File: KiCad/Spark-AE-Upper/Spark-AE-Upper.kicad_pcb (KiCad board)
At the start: 2 copper layers, 0 parts

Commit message: bumping copyright year
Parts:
- added RP1: RK09K1130D62, easyeda2kicad:RES-TH_RK09K1130AAU, F.Cu at (125.5, 77.5)
- added RP2: RK09K1130D62, easyeda2kicad:RES-TH_RK09K1130AAU, F.Cu at (139.5, 77.5)

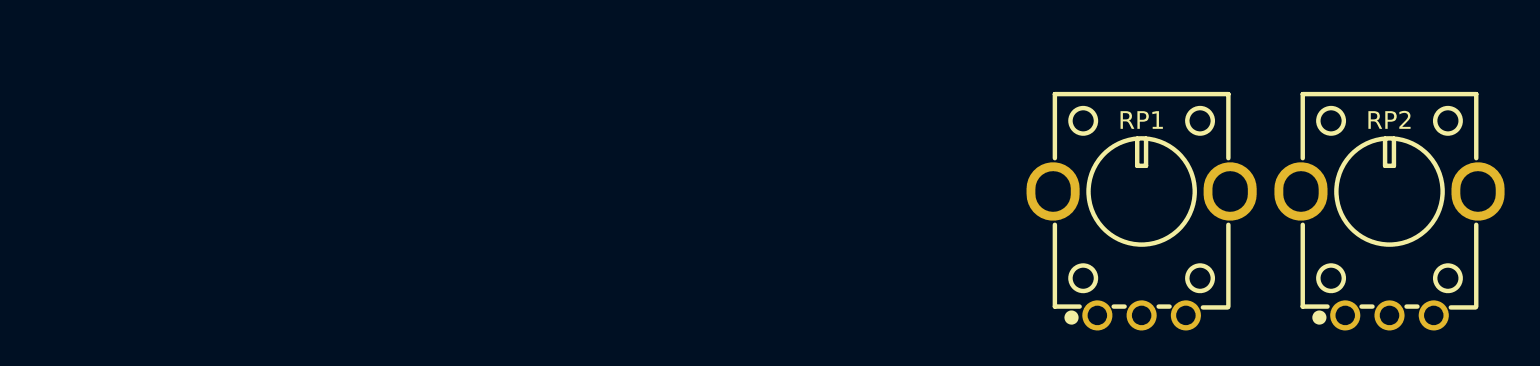
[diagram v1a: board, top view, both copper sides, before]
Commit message: updated to use components from clectric-diy's library
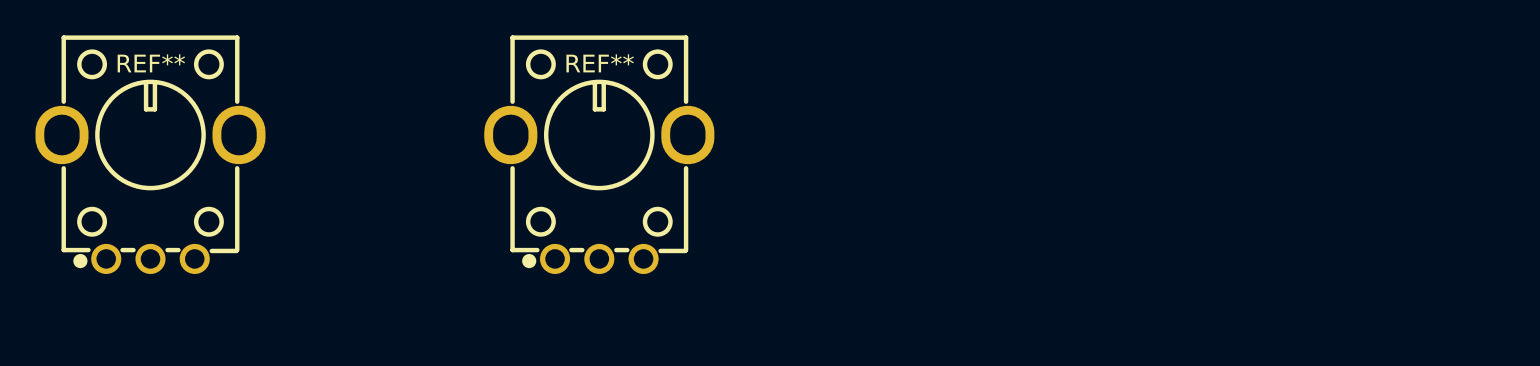
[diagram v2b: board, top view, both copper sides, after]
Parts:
- removed RP1, RP2: RK09K1130D62, easyeda2kicad:RES-TH_RK09K1130AAU
- added REF**: RES-TH_RK09K1130AAU, clectric-diy:RES-TH_RK09K1130AAU, F.Cu at (94.9, 74.3)
- added REF**: RES-TH_RK09K1130AAU, clectric-diy:RES-TH_RK09K1130AAU, F.Cu at (69.5, 74.3)
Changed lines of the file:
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@@
 	)
 	(net 0 "")
-	(net 1 "unconnected-(RP1-Pad2)")
-	(net 2 "unconnected-(RP1-Pad5)")
-	(net 3 "unconnected-(RP1-Pad1)")
-	(net 4 "unconnected-(RP1-Pad4)")
-	(net 5 "unconnected-(RP1-Pad3)")
-	(net 6 "unconnected-(RP2-Pad4)")
-	(net 7 "unconnected-(RP2-Pad1)")
-	(net 8 "unconnected-(RP2-Pad5)")
-	(net 9 "unconnected-(RP2-Pad3)")
-	(net 10 "unconnected-(RP2-Pad2)")
-	(footprint "easyeda2kicad:RES-TH_RK09K1130AAU"
+	(footprint "clectric-diy:RES-TH_RK09K1130AAU"
 		(layer "F.Cu")
-		(at 125.5 77.5)
-		(property "Reference" "RP1"
+		(at 94.87 74.31)
+		(property "Reference" "REF**"
 			(at 0 -7.5 0)
 			(layer "F.SilkS")
@@
 			)
 		)
-		(property "Value" "RK09K1130D62"
+		(property "Value" "RES-TH_RK09K1130AAU"
 			(at 0 7.5 0)
 			(layer "F.Fab")
@@
 			)
 		)
-		(property "LCSC Part" "C470399"
-			(at 0 0 0)
-			(unlocked yes)
-			(layer "F.Fab")
-			(hide yes)
-			(effects
-				(font
-					(size 1 1)
-					(thickness 0.15)
-				)
-			)
-		)
-		(sheetname "/")
-		(sheetfile "Spark-AE-Upper.kicad_sch")
 		(attr through_hole)
 		(fp_line
@@
 			(layers "*.Cu" "*.Mask")
 			(remove_unused_layers no)
-			(net 3 "unconnected-(RP1-Pad1)")
-			(pinfunction "1")
-			(pintype "unspecified")
 		)
 		(pad "2" thru_hole circle
@@
 			(layers "*.Cu" "*.Mask")
 			(remove_unused_layers no)
-			(net 1 "unconnected-(RP1-Pad2)")
-			(pinfunction "2")
-			(pintype "unspecified")
 		)
 		(pad "3" thru_hole circle
@@
 			(layers "*.Cu" "*.Mask")
 			(remove_unused_layers no)
-			(net 5 "unconnected-(RP1-Pad3)")
-			(pinfunction "3")
-			(pintype "unspecified")
 		)
 		(pad "4" thru_hole oval
@@
 			(layers "*.Cu" "*.Mask")
 			(remove_unused_layers no)
-			(net 4 "unconnected-(RP1-Pad4)")
-			(pinfunction "4")
-			(pintype "unspecified")
 		)
 		(pad "5" thru_hole oval
@@
 			(layers "*.Cu" "*.Mask")
 			(remove_unused_layers no)
-			(net 2 "unconnected-(RP1-Pad5)")
-			(pinfunction "5")
-			(pintype "unspecified")
 		)
 		(embedded_fonts no)
@@
 		)
 	)
-	(footprint "easyeda2kicad:RES-TH_RK09K1130AAU"
+	(footprint "clectric-diy:RES-TH_RK09K1130AAU"
 		(layer "F.Cu")
-		(at 139.5 77.5)
-		(property "Reference" "RP2"
+		(at 69.52 74.31)
+		(property "Reference" "REF**"
 			(at 0 -7.5 0)
 			(layer "F.SilkS")
@@
 			)
 		)
-		(property "Value" "RK09K1130D62"
+		(property "Value" "RES-TH_RK09K1130AAU"
 			(at 0 7.5 0)
 			(layer "F.Fab")
@@
 			)
 		)
-		(property "LCSC Part" "C470399"
-			(at 0 0 0)
-			(unlocked yes)
-			(layer "F.Fab")
-			(hide yes)
-			(effects
-				(font
-					(size 1 1)
-					(thickness 0.15)
-				)
-			)
-		)
-		(sheetname "/")
-		(sheetfile "Spark-AE-Upper.kicad_sch")
 		(attr through_hole)
 		(fp_line
@@
 			(layers "*.Cu" "*.Mask")
 			(remove_unused_layers no)
-			(net 7 "unconnected-(RP2-Pad1)")
-			(pinfunction "1")
-			(pintype "unspecified")
 		)
 		(pad "2" thru_hole circle
@@
 			(layers "*.Cu" "*.Mask")
 			(remove_unused_layers no)
-			(net 10 "unconnected-(RP2-Pad2)")
-			(pinfunction "2")
-			(pintype "unspecified")
 		)
 		(pad "3" thru_hole circle
@@
 			(layers "*.Cu" "*.Mask")
 			(remove_unused_layers no)
-			(net 9 "unconnected-(RP2-Pad3)")
-			(pinfunction "3")
-			(pintype "unspecified")
 		)
 		(pad "4" thru_hole oval
@@
 			(layers "*.Cu" "*.Mask")
 			(remove_unused_layers no)
-			(net 6 "unconnected-(RP2-Pad4)")
-			(pinfunction "4")
-			(pintype "unspecified")
 		)
 		(pad "5" thru_hole oval
@@
 			(layers "*.Cu" "*.Mask")
 			(remove_unused_layers no)
-			(net 8 "unconnected-(RP2-Pad5)")
-			(pinfunction "5")
-			(pintype "unspecified")
 		)
 		(embedded_fonts no)

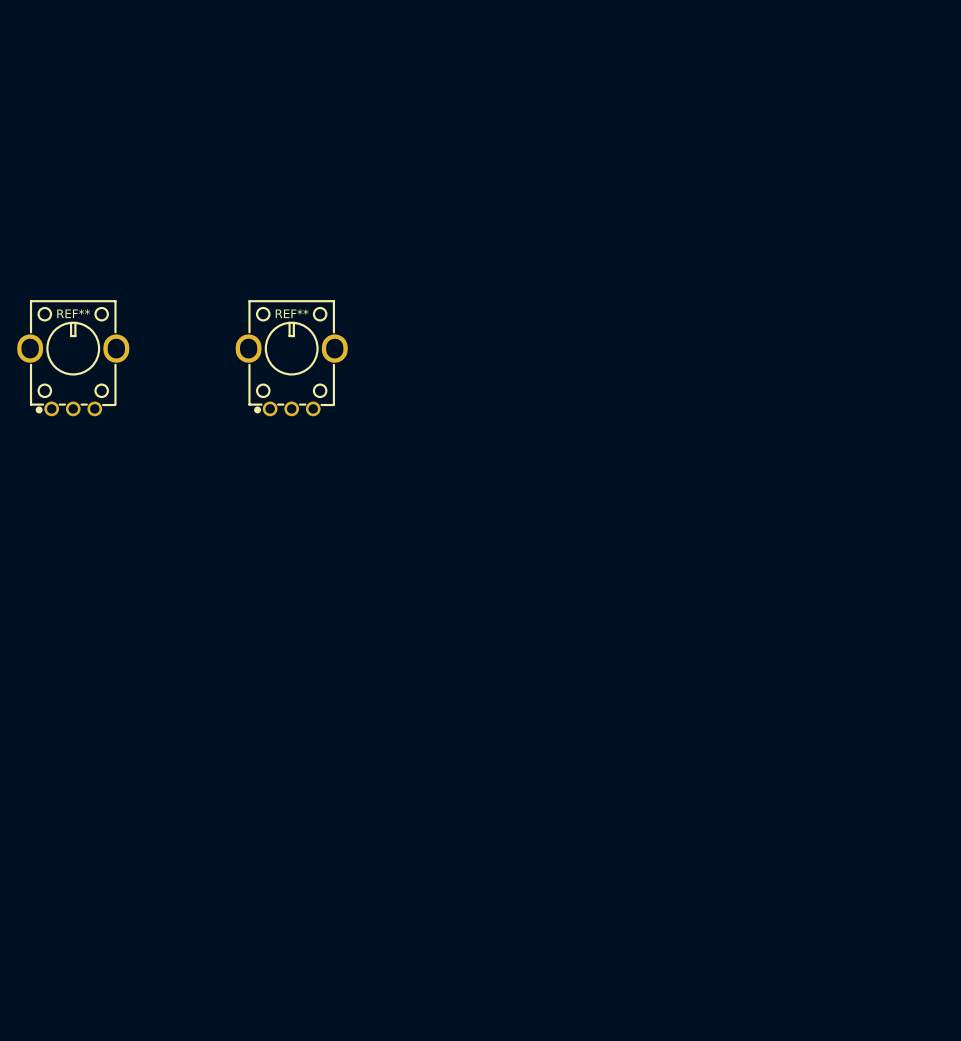
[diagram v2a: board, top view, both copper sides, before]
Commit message: laid out upper board interface and connections
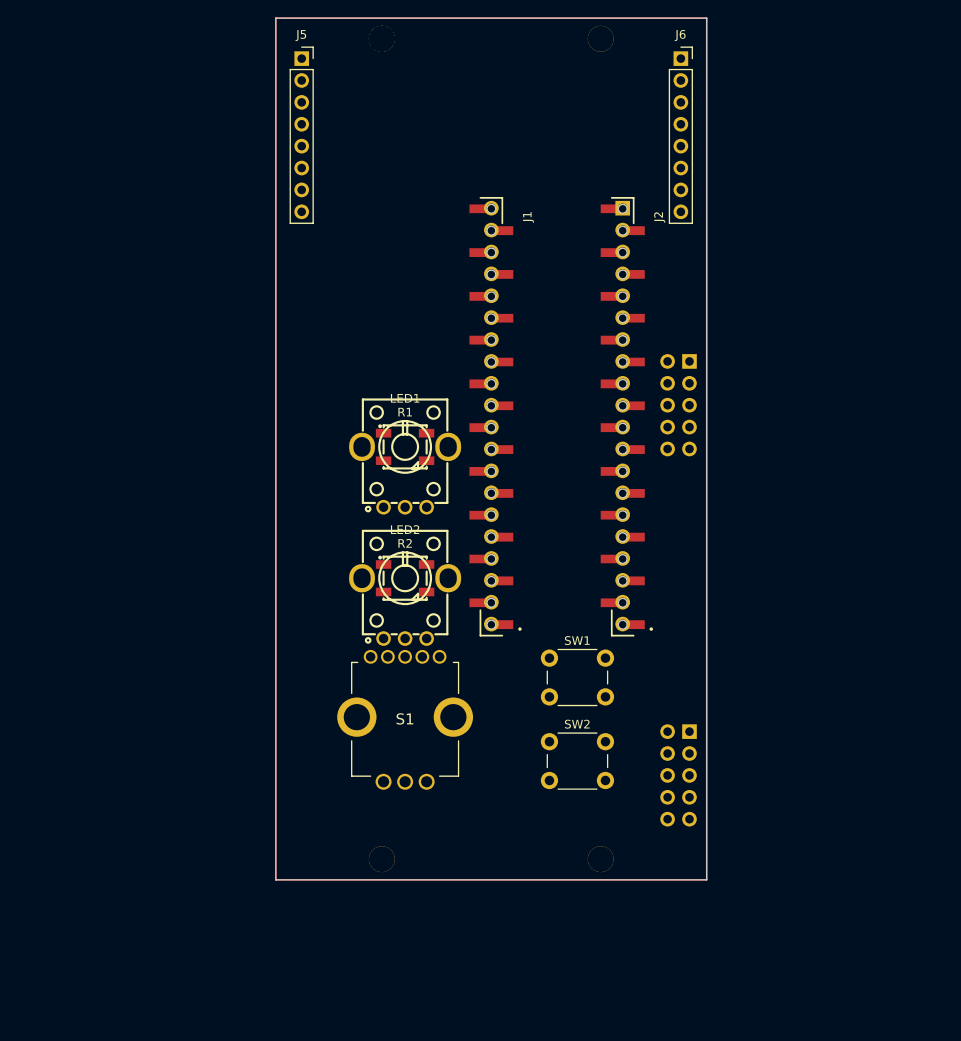
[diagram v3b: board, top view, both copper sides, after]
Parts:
- removed REF** (x2): RES-TH_RK09K1130AAU, clectric-diy:RES-TH_RK09K1130AAU
- added ? (x2): , , F.Cu at (105.3, 34.9)
- added ?: , , F.Cu at (105.3, 130.1)
- added ?: , , F.Cu at (130.7, 130.1)
- added ?: , , F.Cu at (130.7, 34.9)
- added A1: Electrosmith_Daisy_Seed_Rev4, Module:Electrosmith_Daisy_Seed, B.Cu at (133.3, 54.5)
- added J1: SSM-120-L-SV-BE, clectric-diy:SAMTEC_SSM-120-L-SV-BE, F.Cu at (118.0, 78.7)
- added J2: SSM-120-L-SV-BE, clectric-diy:SAMTEC_SSM-120-L-SV-BE, F.Cu at (133.3, 78.7)
- added J3: Conn_02x05_Odd_Even, Connector_PinHeader_2.54mm:PinHeader_2x05_P2.54mm_Vertical, B.Cu at (141.0, 72.3)
- added J4: Conn_02x05_Odd_Even, Connector_PinHeader_2.54mm:PinHeader_2x05_P2.54mm_Vertical, B.Cu at (141.0, 115.3)
- added J5: Conn_01x08_Socket, Connector_PinSocket_2.54mm:PinSocket_1x08_P2.54mm_Vertical, F.Cu at (96.0, 37.2)
- added J6: Conn_01x08_Socket, Connector_PinSocket_2.54mm:PinSocket_1x08_P2.54mm_Vertical, F.Cu at (140.0, 37.2)
- added LED1: WS2812B-V5/W, clectric-diy:LED-SMD_4P-L5.0-W5.0-TL-1, F.Cu at (108.0, 82.2)
- added LED2: WS2812B-V5/W, clectric-diy:LED-SMD_4P-L5.0-W5.0-TL-1, F.Cu at (108.0, 97.5)
- added R1: RK09K1130A8G, clectric-diy:RES-TH_RK09K113004U, F.Cu at (108.0, 85.7)
- added R2: RK09K1130A8G, clectric-diy:RES-TH_RK09K113004U, F.Cu at (108.0, 101.0)
- added S1: PEL12T-4225S-S1024, clectric-diy:PEL12T4225SS1024, F.Cu at (108.0, 113.8)
- added SW1: SW_Push, Button_Switch_THT:SW_PUSH_6mm, F.Cu at (124.8, 106.7)
- added SW2: SW_Push, Button_Switch_THT:SW_PUSH_6mm, F.Cu at (124.8, 116.4)
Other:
- board outline added: 50 x 100 mm

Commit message: added and connected nets for daisy seed socket
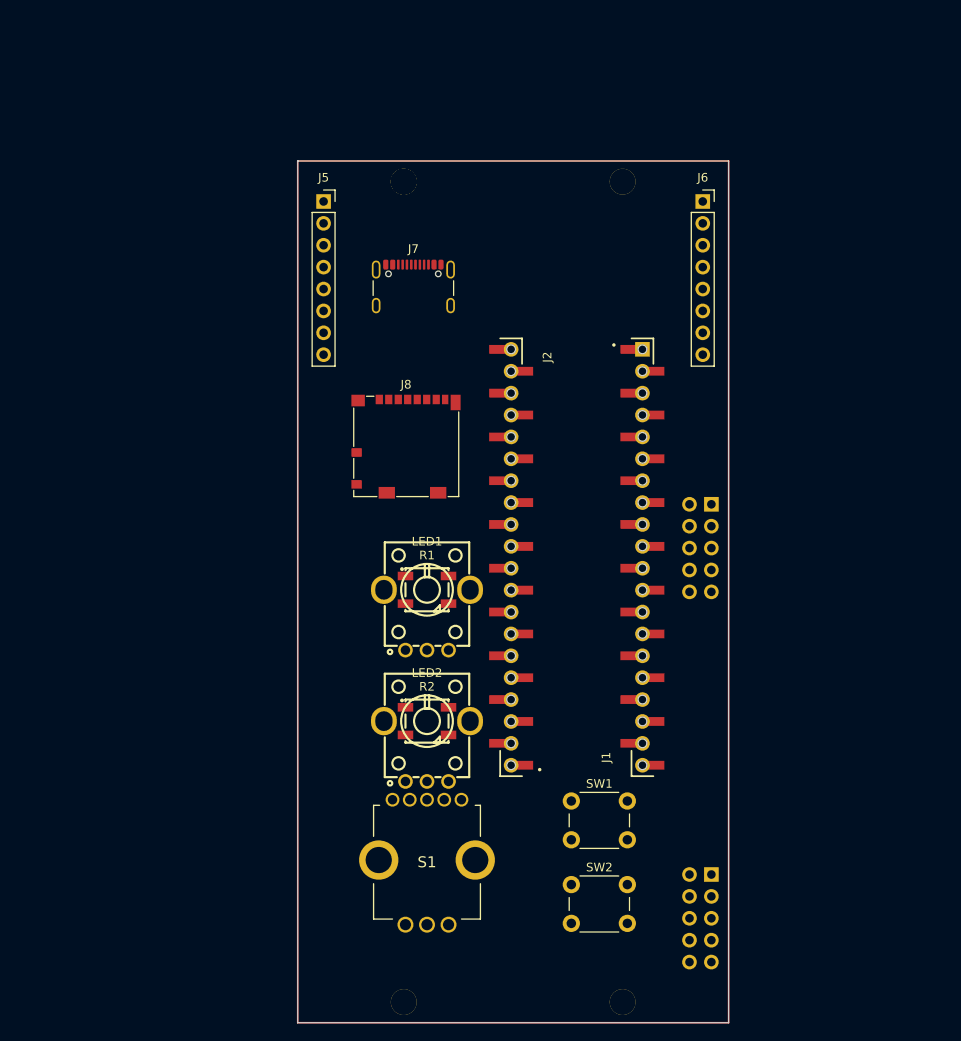
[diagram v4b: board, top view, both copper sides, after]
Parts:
- added J7: USB_C_Receptacle, Connector_USB:USB_C_Receptacle_GCT_USB4105-xx-A_16P_TopMnt_Horizontal, F.Cu at (109.0, 64.7)
- added J8: Micro_SD_Card_Det1, Connector_Card:microSD_HC_Molex_104031-0811, F.Cu at (108.1, 82.2)
- moved J1 23.9 mm to (135.6, 95.0), turned to 90 degrees
- moved J2 20.8 mm to (120.3, 95.0)
- moved LED2 16.8 mm to (110.6, 114.0)
- moved R2 16.8 mm to (110.6, 117.5)
- moved J5 16.8 mm to (98.6, 53.7)
- moved J6 16.8 mm to (142.6, 53.7)
- moved ? 16.8 mm to (133.3, 51.4)
- moved ? 16.8 mm to (107.9, 51.4) (x2)
- moved J3 16.8 mm to (143.6, 88.9)
- moved J4 16.8 mm to (143.6, 131.8)
- moved LED1 16.8 mm to (110.6, 98.8)
- moved R1 16.8 mm to (110.6, 102.3)
- moved S1 16.8 mm to (110.6, 130.4)
- moved SW1 16.8 mm to (127.3, 123.3)
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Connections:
- A1 pad 1: unconnected-(A1-USB_ID-Pad1) -> D0
- A1 pad 10: unconnected-(A1-SPI1_POCI-Pad10) -> D9
- A1 pad 11: unconnected-(A1-SPI1_PICO-Pad11) -> D10
- A1 pad 12: unconnected-(A1-I2C1_SCL-Pad12) -> D11
- A1 pad 13: unconnected-(A1-I2C1_SDA-Pad13) -> D12
- A1 pad 14: unconnected-(A1-USART1_TX-Pad14) -> D13
- A1 pad 15: unconnected-(A1-USART1_RX-Pad15) -> D14
- A1 pad 16: unconnected-(A1-AUDIO_IN_1-Pad16) -> AUDIO_IN_1
- A1 pad 17: unconnected-(A1-AUDIO_IN_2-Pad17) -> AUDIO_IN_2
- A1 pad 18: unconnected-(A1-AUDIO_OUT_1-Pad18) -> AUDIO_OUT_1
- A1 pad 19: unconnected-(A1-AUDIO_OUT_2-Pad19) -> AUDIO_OUT_2
- A1 pad 2: unconnected-(A1-SD_DATA_3-Pad2) -> D1
- A1 pad 20: unconnected-(A1-AGND-Pad20) -> AGND
- A1 pad 21: unconnected-(A1-3V3_A-Pad21) -> 3V3_A
- A1 pad 22: unconnected-(A1-ADC_0-Pad22) -> A0_D15
- A1 pad 23: unconnected-(A1-ADC_1-Pad23) -> A1_D16
- A1 pad 24: unconnected-(A1-ADC_2-Pad24) -> A2_D17
- A1 pad 25: unconnected-(A1-ADC_3-Pad25) -> A3_D18
- A1 pad 26: unconnected-(A1-ADC_4-Pad26) -> A4_D19
- A1 pad 27: unconnected-(A1-ADC_5-Pad27) -> A5_D20
- A1 pad 28: unconnected-(A1-ADC_6-Pad28) -> A6_D21
- A1 pad 29: unconnected-(A1-DAC_OUT2-Pad29) -> A7_D22
- A1 pad 3: unconnected-(A1-SD_DATA_2-Pad3) -> D2
- A1 pad 30: unconnected-(A1-DAC_OUT1-Pad30) -> A8_D23
- A1 pad 31: unconnected-(A1-SAI2_MCLK-Pad31) -> A9_D24
- A1 pad 32: unconnected-(A1-SAI2_SD_B-Pad32) -> A10_D25
- A1 pad 33: unconnected-(A1-SAI2_SD_A-Pad33) -> D26
- A1 pad 34: unconnected-(A1-SAI2_FS-Pad34) -> D27
- A1 pad 35: unconnected-(A1-SAI2_SCK-Pad35) -> A11_D28
- A1 pad 36: unconnected-(A1-USB_D_--Pad36) -> D29
- A1 pad 37: unconnected-(A1-USB_D_+-Pad37) -> D30
- A1 pad 38: unconnected-(A1-3V3_D-Pad38) -> 3V3_D
- A1 pad 39: unconnected-(A1-VIN-Pad39) -> VIN
- A1 pad 4: unconnected-(A1-SD_DATA_1-Pad4) -> D3
- A1 pad 40: unconnected-(A1-DGND-Pad40) -> DGND
- A1 pad 5: unconnected-(A1-SD_DATA_0-Pad5) -> D4
- A1 pad 6: unconnected-(A1-SD_CMD-Pad6) -> D5
- A1 pad 7: unconnected-(A1-SD_CLK-Pad7) -> D6
- A1 pad 8: unconnected-(A1-SPI1_CS-Pad8) -> D7
- A1 pad 9: unconnected-(A1-SPI1_SCK-Pad9) -> D8
- J1 pad 01: unconnected-(J1-Pad01) -> D0
- J1 pad 02: unconnected-(J1-Pad02) -> D1
- J1 pad 03: unconnected-(J1-Pad03) -> D2
- J1 pad 04: unconnected-(J1-Pad04) -> D3
- J1 pad 05: unconnected-(J1-Pad05) -> D4
- J1 pad 06: unconnected-(J1-Pad06) -> D5
- J1 pad 07: unconnected-(J1-Pad07) -> D6
- J1 pad 08: unconnected-(J1-Pad08) -> D7
- J1 pad 09: unconnected-(J1-Pad09) -> D8
- J1 pad 10: unconnected-(J1-Pad10) -> D9
- J1 pad 11: unconnected-(J1-Pad11) -> D10
- J1 pad 12: unconnected-(J1-Pad12) -> D11
- J1 pad 13: unconnected-(J1-Pad13) -> D12
- J1 pad 14: unconnected-(J1-Pad14) -> D13
- J1 pad 15: unconnected-(J1-Pad15) -> D14
- J1 pad 16: unconnected-(J1-Pad16) -> AUDIO_IN_1
- J1 pad 17: unconnected-(J1-Pad17) -> AUDIO_IN_2
- J1 pad 18: unconnected-(J1-Pad18) -> AUDIO_OUT_1
- J1 pad 19: unconnected-(J1-Pad19) -> AUDIO_OUT_2
- J1 pad 20: unconnected-(J1-Pad20) -> AGND
- J2 pad 01: unconnected-(J2-Pad01) -> 3V3_A
- J2 pad 02: unconnected-(J2-Pad02) -> A0_D15
- J2 pad 03: unconnected-(J2-Pad03) -> A1_D16
- J2 pad 04: unconnected-(J2-Pad04) -> A2_D17
- J2 pad 05: unconnected-(J2-Pad05) -> A3_D18
- J2 pad 06: unconnected-(J2-Pad06) -> A4_D19
- J2 pad 07: unconnected-(J2-Pad07) -> A5_D20
- J2 pad 08: unconnected-(J2-Pad08) -> A6_D21
- J2 pad 09: unconnected-(J2-Pad09) -> A7_D22
- J2 pad 10: unconnected-(J2-Pad10) -> A8_D23
- J2 pad 11: unconnected-(J2-Pad11) -> A9_D24
- J2 pad 12: unconnected-(J2-Pad12) -> A10_D25
- J2 pad 13: unconnected-(J2-Pad13) -> D26
- J2 pad 14: unconnected-(J2-Pad14) -> D27
- J2 pad 15: unconnected-(J2-Pad15) -> A11_D28
- J2 pad 16: unconnected-(J2-Pad16) -> D29
- J2 pad 17: unconnected-(J2-Pad17) -> D30
- J2 pad 18: unconnected-(J2-Pad18) -> 3V3_D
- J2 pad 19: unconnected-(J2-Pad19) -> VIN
- J2 pad 20: unconnected-(J2-Pad20) -> DGND
- LED1 pad 1: unconnected-(LED1-VDD-Pad1) -> Net-(LED1-DIN)
- LED1 pad 3: unconnected-(LED1-DIN-Pad3) -> Net-(LED1-DIN)

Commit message: updated footprints and models
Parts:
- removed J8: Micro_SD_Card_Det1, Connector_Card:microSD_HC_Molex_104031-0811
- added U1: PJS008U-3000-0, clectric-diy:PJS008U-3000-0, F.Cu at (107.8, 82.0)
- A1: footprint Module:Electrosmith_Daisy_Seed -> clectric-diy:DAISY_SEED
